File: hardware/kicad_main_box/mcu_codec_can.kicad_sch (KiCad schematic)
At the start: 3 parts, among them U2 ESP32-S3-WROOM-1-N16R8, U3 ES8388, U6 TCAN334G

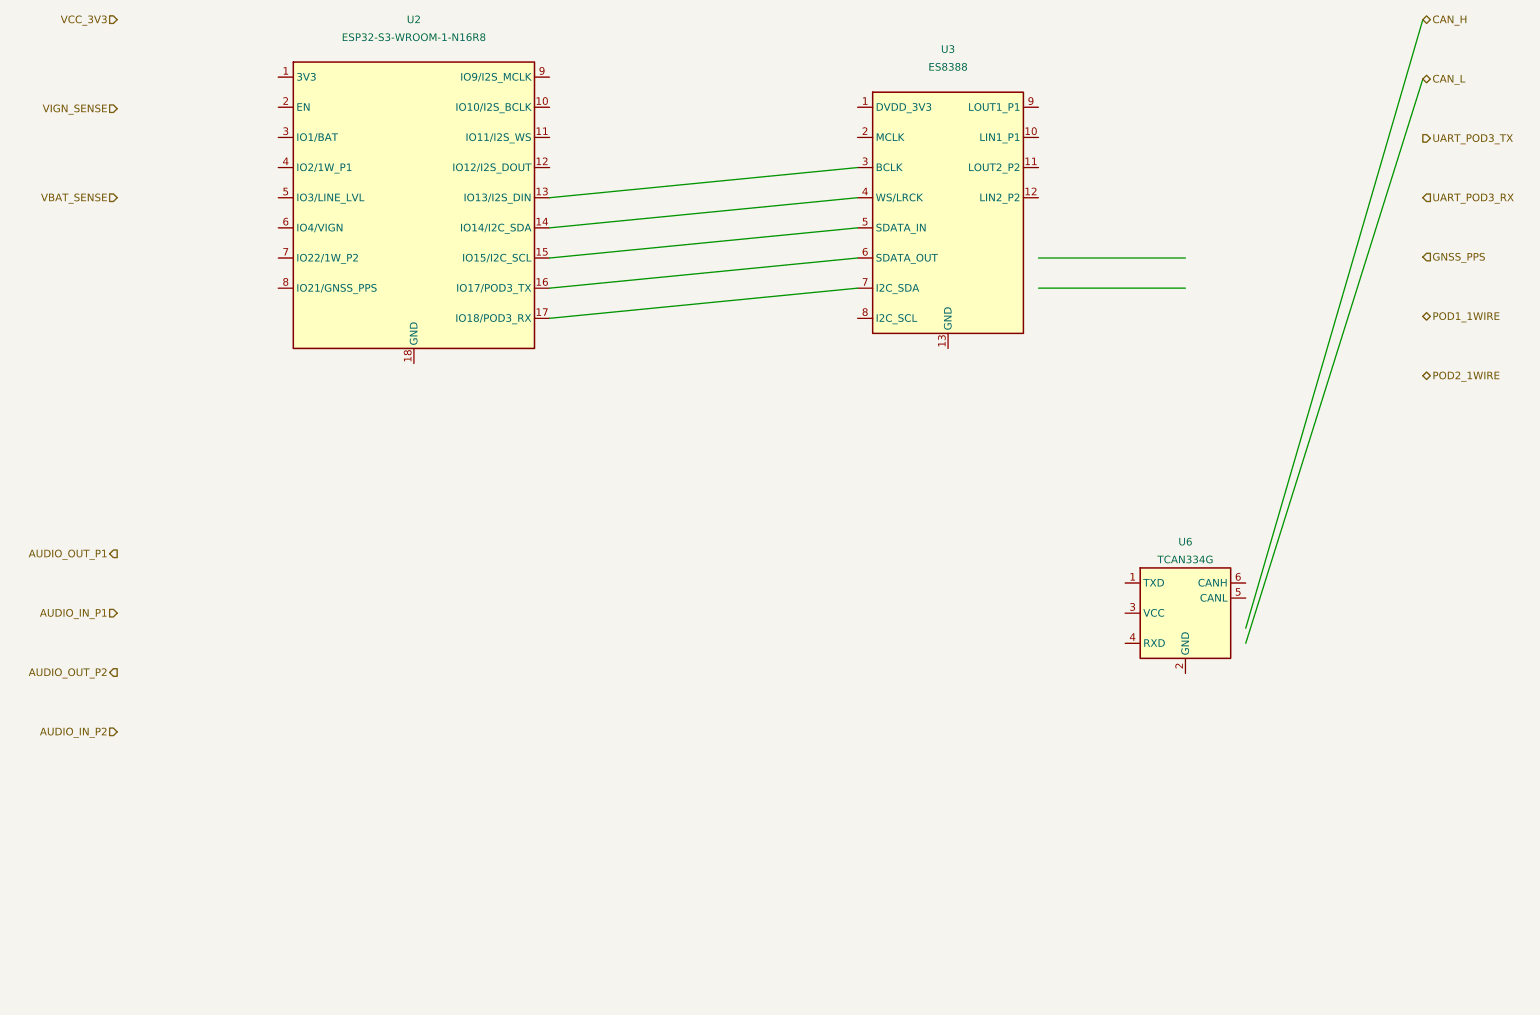
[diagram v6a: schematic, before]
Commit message: fix(main_box): clean up schematics, connect LoRa/UWB/IMU/SD/LED nets, verify J2 MicroSD placement
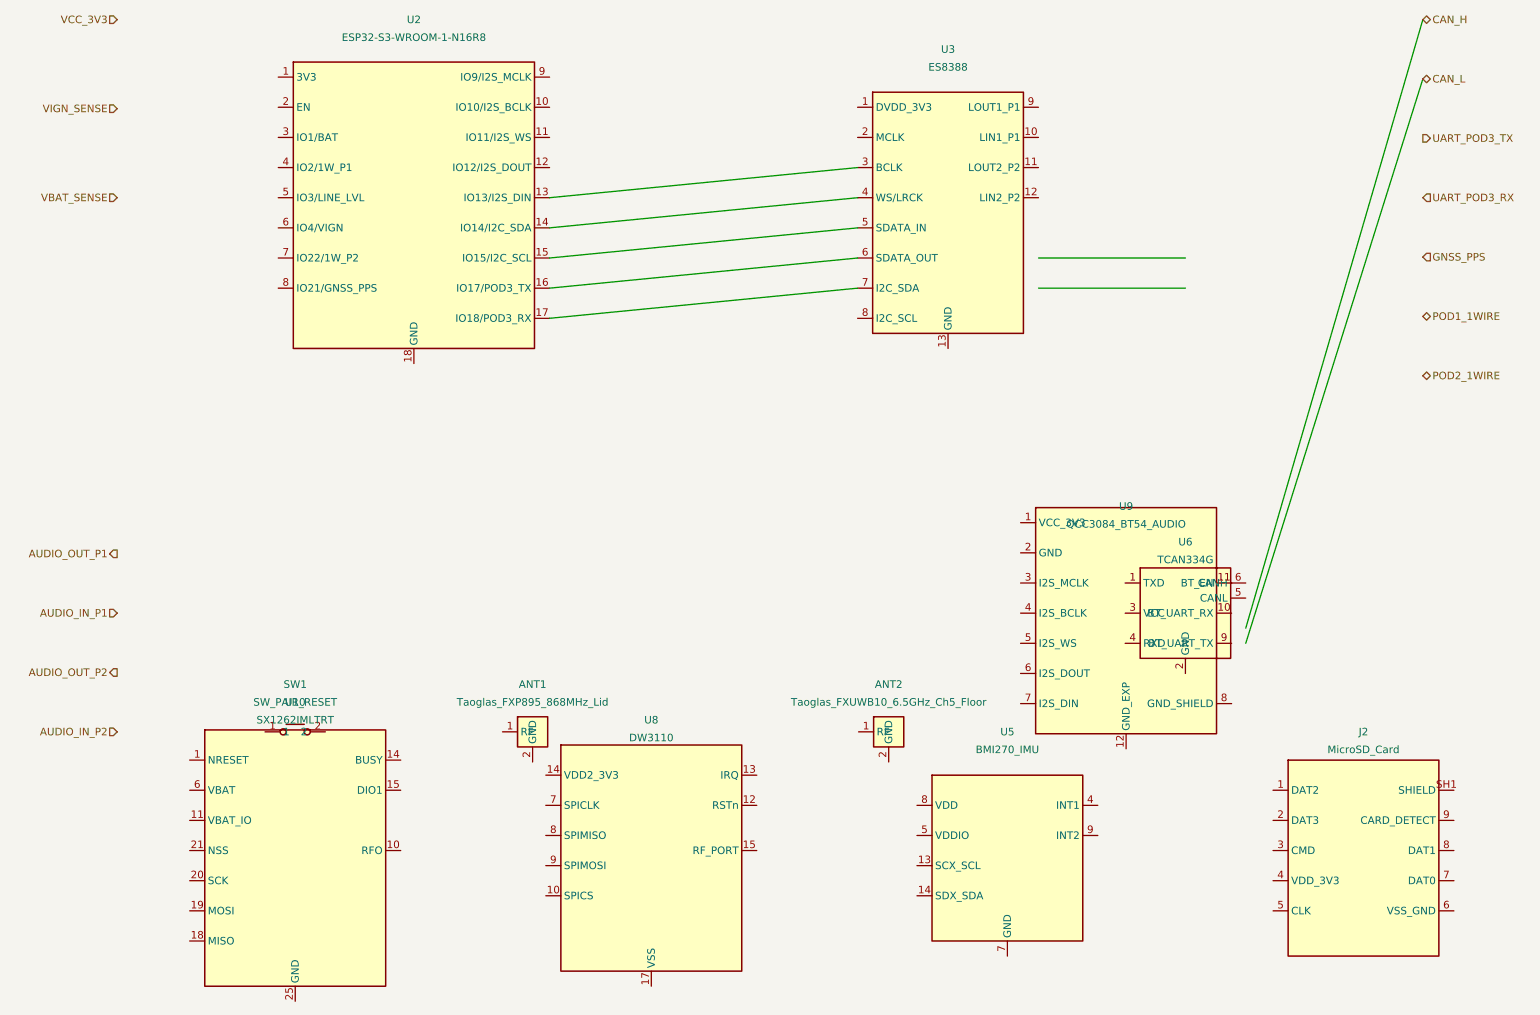
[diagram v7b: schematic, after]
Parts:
- added ANT1: Taoglas_FXP895_868MHz_Lid, Connector_Coaxial:U.FL_Hirose_U.FL-R-SMT-1_Vertical, symbol Connector:U.FL
- added ANT2: Taoglas_FXUWB10_6.5GHz_Ch5_Floor, Connector_Coaxial:U.FL_Hirose_U.FL-R-SMT-1_Vertical, symbol Connector:U.FL
- added J2: MicroSD_Card, Connector_Card:microSD_HC_Hirose_DM3D-SF, symbol Connector:MicroSD_Card
- added SW1: SW_PAIR_RESET, Button_Switch_SMD:SW_Push_SPST_NO_Alps_SKRK, symbol Switch:SW_Push
- added U10: SX1262IMLTRT, QFN-24-1EP_4x4mm_P0.5mm_EP2.8x2.8mm, symbol RF_Module:SX1262
- added U5: BMI270_IMU, Package_LGA:LGA-14_2.5x3mm_P0.5mm, symbol Sensor_Motion:BMI270
- added U8: DW3110, Package_DFN_QFN:QFN-16-1EP_3x3mm_P0.5mm_EP1.7x1.7mm_ThermalVias, symbol RF_Module:DW3110
- added U9: QCC3084_BT54_AUDIO, RF_Module:Qualcomm_QCC3084_Module, symbol RF_Module:Qualcomm_QCC3084_Module
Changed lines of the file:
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@@
+		)
+	)
+		(symbol (lib_id "RF_Module:Qualcomm_QCC3084_Module") (at 200.0 140.0 0) (unit 1)
+		(in_bom yes) (on_board yes) (dnp no)
+		(property "Reference" "U9" (at 200.0 122.0 0) (effects (font (size 1.27 1.27))))
+		(property "Value" "QCC3084_BT54_AUDIO" (at 200.0 125.0 0) (effects (font (size 1.27 1.27))))
+		(property "Footprint" "RF_Module:Qualcomm_QCC3084_Module" (at 0 0 0) (effects (font (size 1.27 1.27)) (hide yes)))
+		(property "LCSC" "C983084" (at 0 0 0) (effects (font (size 1.27 1.27)) (hide yes)))
+		(pin "1")
+		(pin "2")
+		(pin "3")
+		(pin "4")
+		(pin "5")
+		(pin "6")
+		(pin "7")
+		(pin "8")
+		(pin "9")
+		(pin "10")
+		(pin "11")
+		(instances
+			(project "openmotorbridge_main"
+				(path "/a0000000-0000-0000-0000-000000000001/a0000000-0000-0000-0000-000000000003"
+					(reference "U9")
+					(unit 1)
+				)
+			)
+		)
+	)
+	(symbol (lib_id "RF_Module:SX1262") (at 60 180 0) (unit 1)
+		(in_bom yes) (on_board yes) (dnp no)
+		(property "Reference" "U10" (at 60 155 0) (effects (font (size 1.27 1.27))))
+		(property "Value" "SX1262IMLTRT" (at 60 158 0) (effects (font (size 1.27 1.27))))
+		(property "Footprint" "QFN-24-1EP_4x4mm_P0.5mm_EP2.8x2.8mm" (at 0 0 0) (effects (font (size 1.27 1.27)) hide))
+		(instances
+			(project "openmotorbridge_main"
+				(path "/a0000000-0000-0000-0000-000000000001/a0000000-0000-0000-0000-000000000003"
+					(reference "U10")
+					(unit 1)
+				)
+			)
+		)
+	)
+	(symbol (lib_id "RF_Module:DW3110") (at 120 180 0) (unit 1)
+		(in_bom yes) (on_board yes) (dnp no)
+		(property "Reference" "U8" (at 120 158 0) (effects (font (size 1.27 1.27))))
+		(property "Value" "DW3110" (at 120 161 0) (effects (font (size 1.27 1.27))))
+		(property "Footprint" "Package_DFN_QFN:QFN-16-1EP_3x3mm_P0.5mm_EP1.7x1.7mm_ThermalVias" (at 0 0 0) (effects (font (size 1.27 1.27)) hide))
+		(instances
+			(project "openmotorbridge_main"
+				(path "/a0000000-0000-0000-0000-000000000001/a0000000-0000-0000-0000-000000000003"
+					(reference "U8")
+					(unit 1)
+				)
+			)
+		)
+	)
+	(symbol (lib_id "Sensor_Motion:BMI270") (at 180 180 0) (unit 1)
+		(in_bom yes) (on_board yes) (dnp no)
+		(property "Reference" "U5" (at 180 160 0) (effects (font (size 1.27 1.27))))
+		(property "Value" "BMI270_IMU" (at 180 163 0) (effects (font (size 1.27 1.27))))
+		(property "Footprint" "Package_LGA:LGA-14_2.5x3mm_P0.5mm" (at 0 0 0) (effects (font (size 1.27 1.27)) hide))
+		(instances
+			(project "openmotorbridge_main"
+				(path "/a0000000-0000-0000-0000-000000000001/a0000000-0000-0000-0000-000000000003"
+					(reference "U5")
+					(unit 1)
+				)
+			)
+		)
+	)
+	(symbol (lib_id "Connector:MicroSD_Card") (at 240 180 0) (unit 1)
+		(in_bom yes) (on_board yes) (dnp no)
+		(property "Reference" "J2" (at 240 160 0) (effects (font (size 1.27 1.27))))
+		(property "Value" "MicroSD_Card" (at 240 163 0) (effects (font (size 1.27 1.27))))
+		(property "Footprint" "Connector_Card:microSD_HC_Hirose_DM3D-SF" (at 0 0 0) (effects (font (size 1.27 1.27)) hide))
+		(instances
+			(project "openmotorbridge_main"
+				(path "/a0000000-0000-0000-0000-000000000001/a0000000-0000-0000-0000-000000000003"
+					(reference "J2")
+					(unit 1)
+				)
+			)
+		)
+	)
+	(symbol (lib_id "Connector:U.FL") (at 100.0 160.0 0) (unit 1)
+		(in_bom yes) (on_board yes) (dnp no)
+		(property "Reference" "ANT1" (at 100.0 152.0 0) (effects (font (size 1.27 1.27))))
+		(property "Value" "Taoglas_FXP895_868MHz_Lid" (at 100.0 155.0 0) (effects (font (size 1.27 1.27))))
+		(property "Footprint" "Connector_Coaxial:U.FL_Hirose_U.FL-R-SMT-1_Vertical" (at 0 0 0) (effects (font (size 1.27 1.27)) (hide yes)))
+		(property "LCSC" "C2834595" (at 0 0 0) (effects (font (size 1.27 1.27)) (hide yes)))
+		(pin "1")
+		(pin "2")
+		(instances
+			(project "openmotorbridge_main"
+				(path "/a0000000-0000-0000-0000-000000000001/a0000000-0000-0000-0000-000000000003"
+					(reference "ANT1")
+					(unit 1)
+				)
+			)
+		)
+	)
+	(symbol (lib_id "Connector:U.FL") (at 160.0 160.0 0) (unit 1)
+		(in_bom yes) (on_board yes) (dnp no)
+		(property "Reference" "ANT2" (at 160.0 152.0 0) (effects (font (size 1.27 1.27))))
+		(property "Value" "Taoglas_FXUWB10_6.5GHz_Ch5_Floor" (at 160.0 155.0 0) (effects (font (size 1.27 1.27))))
+		(property "Footprint" "Connector_Coaxial:U.FL_Hirose_U.FL-R-SMT-1_Vertical" (at 0 0 0) (effects (font (size 1.27 1.27)) (hide yes)))
+		(property "LCSC" "C2834595" (at 0 0 0) (effects (font (size 1.27 1.27)) (hide yes)))
+		(pin "1")
+		(pin "2")
+		(instances
+			(project "openmotorbridge_main"
+				(path "/a0000000-0000-0000-0000-000000000001/a0000000-0000-0000-0000-000000000003"
+					(reference "ANT2")
+					(unit 1)
+				)
+			)
+		)
+	)
+	(symbol (lib_id "Switch:SW_Push") (at 60.0 160.0 0) (unit 1)
+		(in_bom yes) (on_board yes) (dnp no)
+		(property "Reference" "SW1" (at 60.0 152.0 0) (effects (font (size 1.27 1.27))))
+		(property "Value" "SW_PAIR_RESET" (at 60.0 155.0 0) (effects (font (size 1.27 1.27))))
+		(property "Footprint" "Button_Switch_SMD:SW_Push_SPST_NO_Alps_SKRK" (at 0 0 0) (effects (font (size 1.27 1.27)) (hide yes)))
+		(property "LCSC" "C318884" (at 0 0 0) (effects (font (size 1.27 1.27)) (hide yes)))
+		(pin "1")
+		(pin "2")
+		(instances
+			(project "openmotorbridge_main"
+				(path "/a0000000-0000-0000-0000-000000000001/a0000000-0000-0000-0000-000000000003"
+					(reference "SW1")
+					(unit 1)
+				)
+			)
 		)
 	)

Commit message: feat(hw): finalize PCB lineup routing, sync PCBA 03 cartridge with J_PROG header and DTM12 schematics
- PCBA 01 (Central Box): Remediate net routing, DTM12 hierarchical schematic synchronization, 100% routed, 0 DRC errors.
- PCBA 03 (Smart Modular Cartridge): Position and route J_PROG 4-pin SMD programming header on F.Cu at (108.0, 89.61), synchronize CPL and schematic, 100% routed, 0 DRC errors.
- PCBA 05 (Universal Front Node): Preconnect and routing verified, 100% routed, 0 DRC errors.
- PCBA 07 (LoRa Smart-Keyfob): Routing and DRC verified, 100% routed, 0 DRC errors.
- PCBA 08 (Radar 2.0 Sub-MCU & Wings): Sub-MCU routing and HF isolation verified, 100% routed, 0 DRC errors.
- PCBA 10 (OMM 446 PMR/DMR Intercom): KiCad DRC verified, 100% routed, 0 DRC errors.
- Firmware: Align configuration headers across front_node and smart_cartridge.
- Tools: Add comprehensive preflight PCBA audit suite tools/audit_pcbas_preflight.py.
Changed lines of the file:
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@@
 		(title "OpenMotorBridge v8.0 - MCU, Audio Codec & CAN-Bus")
 		(date "2026-08-24")
-		(rev "v8.0")
+		(rev "v9.6")
 		(company "OpenMotorBridge Open Source Hardware")
 		(comment 1 "ESP32-S3-WROOM-1-N16R8 + ES8388 24-Bit Codec + TCAN334G CAN-FD + BMI270 IMU")
@@
 		)
 	)
-	(hierarchical_label "UART_POD3_TX"
-		(shape output)
-		(at 250 60 0)
-		(effects
-			(font
-				(size 1.27 1.27)
-			)
-			(justify left)
-		)
-	)
-	(hierarchical_label "UART_POD3_RX"
-		(shape input)
-		(at 250 70 0)
-		(effects
-			(font
-				(size 1.27 1.27)
-			)
-			(justify left)
-		)
-	)
-	(hierarchical_label "GNSS_PPS"
-		(shape input)
-		(at 250 80 0)
-		(effects
-			(font
-				(size 1.27 1.27)
-			)
-			(justify left)
-		)
-	)
-	(hierarchical_label "POD1_1WIRE"
-		(shape bidirectional)
-		(at 250 90 0)
-		(effects
-			(font
-				(size 1.27 1.27)
-			)
-			(justify left)
-		)
-	)
-	(hierarchical_label "POD2_1WIRE"
-		(shape bidirectional)
-		(at 250 100 0)
-		(effects
-			(font
-				(size 1.27 1.27)
-			)
-			(justify left)
-		)
-	)
-	(hierarchical_label "AUDIO_OUT_P1"
-		(shape output)
-		(at 30 130 180)
-		(effects
-			(font
-				(size 1.27 1.27)
-			)
-			(justify right)
-		)
-	)
-	(hierarchical_label "AUDIO_IN_P1"
-		(shape input)
-		(at 30 140 180)
-		(effects
-			(font
-				(size 1.27 1.27)
-			)
-			(justify right)
-		)
-	)
-	(hierarchical_label "AUDIO_OUT_P2"
-		(shape output)
-		(at 30 150 180)
-		(effects
-			(font
-				(size 1.27 1.27)
-			)
-			(justify right)
-		)
-	)
-	(hierarchical_label "AUDIO_IN_P2"
-		(shape input)
-		(at 30 160 180)
-		(effects
-			(font
-				(size 1.27 1.27)
-			)
-			(justify right)
-		)
-	)
